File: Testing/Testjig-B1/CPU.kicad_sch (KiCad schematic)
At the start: 7 parts

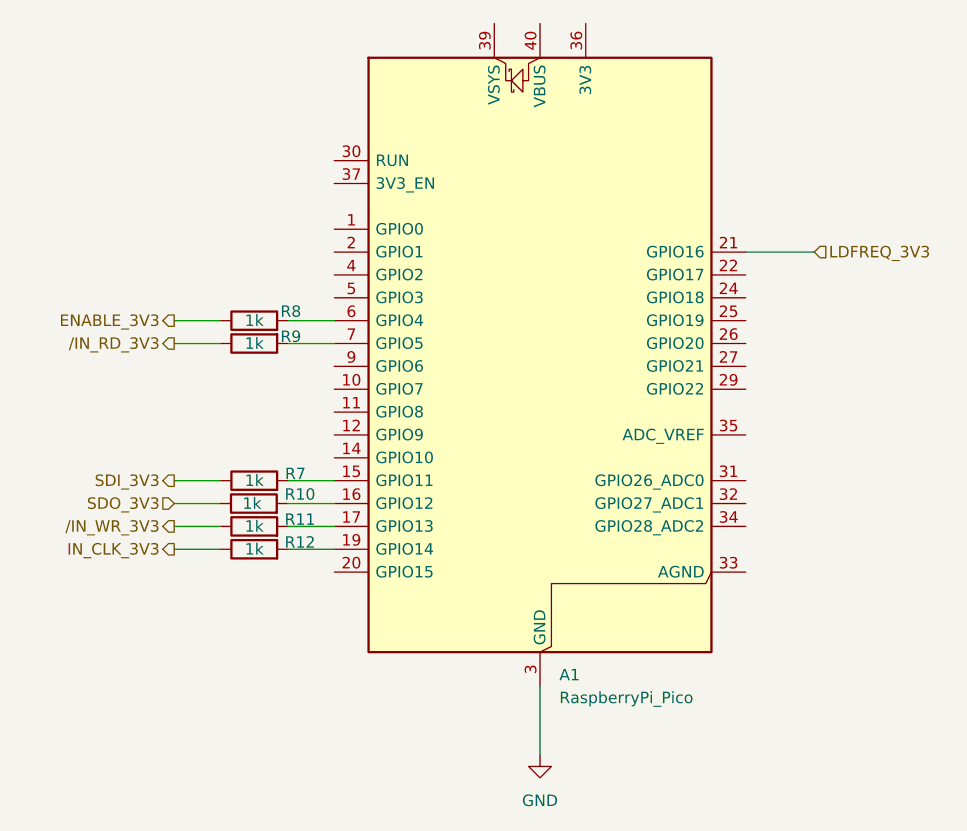
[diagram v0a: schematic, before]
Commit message: First iteration tester design
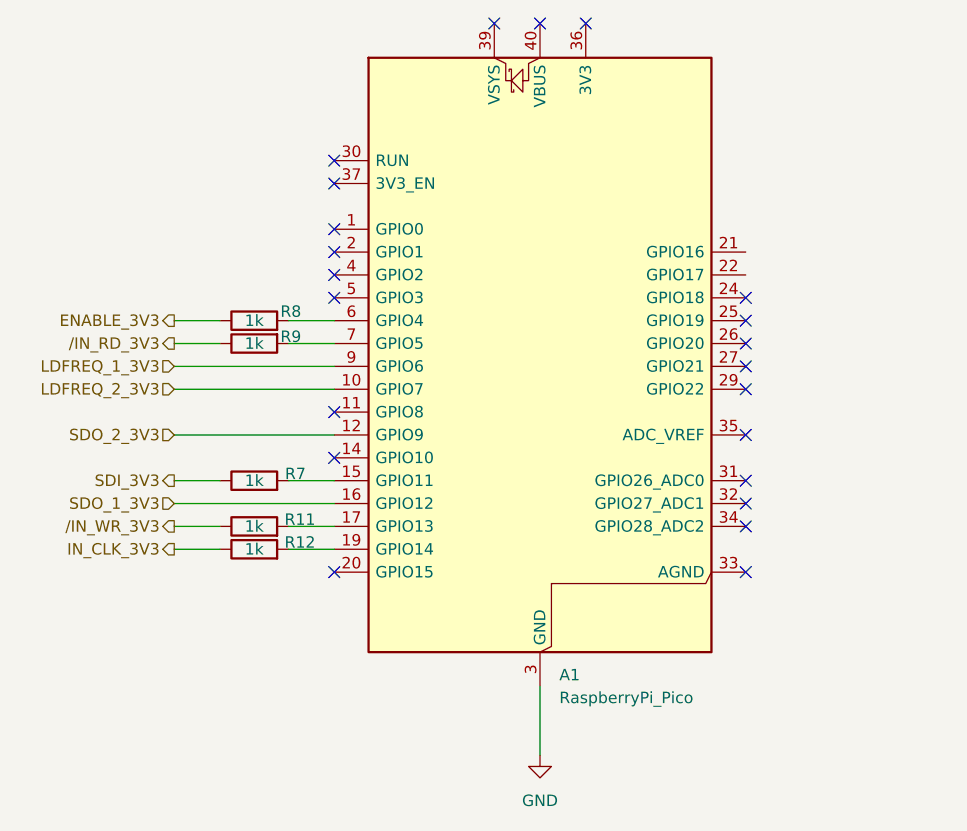
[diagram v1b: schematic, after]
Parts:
- removed R10: 1k, symbol Device:R
- R11, R12, R7, R8, R9: footprint (none) -> Resistor_SMD:R_0805_2012Metric
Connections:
- net LDFREQ_2_3V3: now reaches A1.10 (GPIO7)
- net SDO_2_3V3: now reaches A1.12 (GPIO9)
- net LDFREQ_1_3V3: now reaches A1.9 (GPIO6)
- net LDFREQ_3V3: no longer names the net of A1.21 (GPIO16)
- no-connect marks 0 -> 22
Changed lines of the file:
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@@
 	(generator_version "10.0")
 	(paper "A4")
-	(wire
-		(pts
-			(xy 125.73 69.85) (xy 133.35 69.85)
-		)
-		(stroke
-			(width 0)
-			(type default)
-		)
-	)
-	(wire
-		(pts
-			(xy 74.8862 97.79) (xy 80.01 97.79)
+	(no_connect
+		(at 80.01 69.85)
+	)
+	(no_connect
+		(at 125.73 90.17)
+	)
+	(no_connect
+		(at 125.73 85.09)
+	)
+	(no_connect
+		(at 80.01 87.63)
+	)
+	(no_connect
+		(at 80.01 105.41)
+	)
+	(no_connect
+		(at 107.95 44.45)
+	)
+	(no_connect
+		(at 125.73 77.47)
+	)
+	(no_connect
+		(at 125.73 100.33)
+	)
+	(no_connect
+		(at 125.73 82.55)
+	)
+	(no_connect
+		(at 125.73 80.01)
+	)
+	(no_connect
+		(at 102.87 44.45)
+	)
+	(no_connect
+		(at 125.73 74.93)
+	)
+	(no_connect
+		(at 80.01 59.69)
+	)
+	(no_connect
+		(at 80.01 92.71)
+	)
+	(no_connect
+		(at 80.01 74.93)
+	)
+	(no_connect
+		(at 125.73 97.79)
+	)
+	(no_connect
+		(at 80.01 62.23)
+	)
+	(no_connect
+		(at 80.01 72.39)
+	)
+	(no_connect
+		(at 97.79 44.45)
+	)
+	(no_connect
+		(at 80.01 67.31)
+	)
+	(no_connect
+		(at 125.73 105.41)
+	)
+	(no_connect
+		(at 125.73 95.25)
+	)
+	(wire
+		(pts
+			(xy 80.01 85.09) (xy 62.23 85.09)
 		)
 		(stroke
@@
 	(wire
 		(pts
+			(xy 62.23 90.17) (xy 80.01 90.17)
+		)
+		(stroke
+			(width 0)
+			(type default)
+		)
+	)
+	(wire
+		(pts
+			(xy 80.01 82.55) (xy 62.23 82.55)
+		)
+		(stroke
+			(width 0)
+			(type default)
+		)
+	)
+	(wire
+		(pts
 			(xy 74.93 95.25) (xy 80.01 95.25)
 		)
@@
 		(pts
 			(xy 74.93 80.01) (xy 80.01 80.01)
+		)
+		(stroke
+			(width 0)
+			(type default)
+		)
+	)
+	(wire
+		(pts
+			(xy 67.31 97.79) (xy 80.01 97.79)
 		)
 		(stroke
@@
 		)
 	)
+	(hierarchical_label "LDFREQ_2_3V3"
+		(shape input)
+		(at 62.23 85.09 180)
+		(effects
+			(font
+				(size 1.27 1.27)
+			)
+			(justify right)
+		)
+	)
 	(hierarchical_label "ENABLE_3V3"
 		(shape output)
@@
 		)
 	)
-	(hierarchical_label "LDFREQ_3V3"
+	(hierarchical_label "LDFREQ_1_3V3"
 		(shape input)
-		(at 133.35 69.85 0)
+		(at 62.23 82.55 180)
 		(effects
 			(font
 				(size 1.27 1.27)
 			)
-			(justify left)
+			(justify right)
 		)
 	)
@@
 		)
 	)
-	(hierarchical_label "SDO_3V3"
+	(hierarchical_label "SDO_1_3V3"
 		(shape input)
 		(at 62.23 97.79 180)
@@
 		(shape output)
 		(at 62.23 95.25 180)
+		(effects
+			(font
+				(size 1.27 1.27)
+			)
+			(justify right)
+		)
+	)
+	(hierarchical_label "SDO_2_3V3"
+		(shape input)
+		(at 62.23 90.17 180)
 		(effects
 			(font
@@
 			)
 		)
-		(property "Footprint" ""
+		(property "Footprint" "Resistor_SMD:R_0805_2012Metric"
 			(at 71.12 79.248 90)
 			(hide yes)
@@
 				(path "/ac0bcd9a-6984-47ed-9080-83e8edfb761b/3e980933-0fed-482d-9d01-6233af794343"
 					(reference "R8")
-					(unit 1)
-				)
-			)
-		)
-	)
-	(symbol
-		(lib_id "Device:R")
-		(at 71.0762 97.79 90)
-		(unit 1)
-		(body_style 1)
-		(exclude_from_sim no)
-		(in_bom yes)
-		(on_board yes)
-		(in_pos_files yes)
-		(dnp no)
-		(property "Reference" "R10"
-			(at 76.2 96.774 90)
-			(show_name no)
-			(do_not_autoplace no)
-			(effects
-				(font
-					(size 1.27 1.27)
-				)
-			)
-		)
-		(property "Value" "1k"
-			(at 70.866 97.79 90)
-			(show_name no)
-			(do_not_autoplace no)
-			(effects
-				(font
-					(size 1.27 1.27)
-				)
-			)
-		)
-		(property "Footprint" ""
-			(at 71.0762 99.568 90)
-			(hide yes)
-			(show_name no)
-			(do_not_autoplace no)
-			(effects
-				(font
-					(size 1.27 1.27)
-				)
-			)
-		)
-		(property "Datasheet" ""
-			(at 71.0762 97.79 0)
-			(hide yes)
-			(show_name no)
-			(do_not_autoplace no)
-			(effects
-				(font
-					(size 1.27 1.27)
-				)
-			)
-		)
-		(property "Description" "Resistor"
-			(at 71.0762 97.79 0)
-			(hide yes)
-			(show_name no)
-			(do_not_autoplace no)
-			(effects
-				(font
-					(size 1.27 1.27)
-				)
-			)
-		)
-		(pin "1"
-		)
-		(pin "2"
-		)
-		(instances
-			(project "Testjig-B1"
-				(path "/ac0bcd9a-6984-47ed-9080-83e8edfb761b/3e980933-0fed-482d-9d01-6233af794343"
-					(reference "R10")
 					(unit 1)
 				)
@@
 			)
 		)
-		(property "Footprint" ""
+		(property "Footprint" "Resistor_SMD:R_0805_2012Metric"
 			(at 71.12 102.108 90)
 			(hide yes)
@@
 			)
 		)
-		(property "Footprint" ""
+		(property "Footprint" "Resistor_SMD:R_0805_2012Metric"
 			(at 71.12 78.232 90)
 			(hide yes)
@@
 			)
 		)
-		(property "Footprint" ""
+		(property "Footprint" "Resistor_SMD:R_0805_2012Metric"
 			(at 71.12 104.648 90)
 			(hide yes)
@@
 			)
 		)
-		(property "Footprint" ""
+		(property "Footprint" "Resistor_SMD:R_0805_2012Metric"
 			(at 71.12 97.028 90)
 			(hide yes)

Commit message: Last fixes before production of Rev A.
- Add signal line for SDO1 which had a break in the schematic.
- Route out said signal
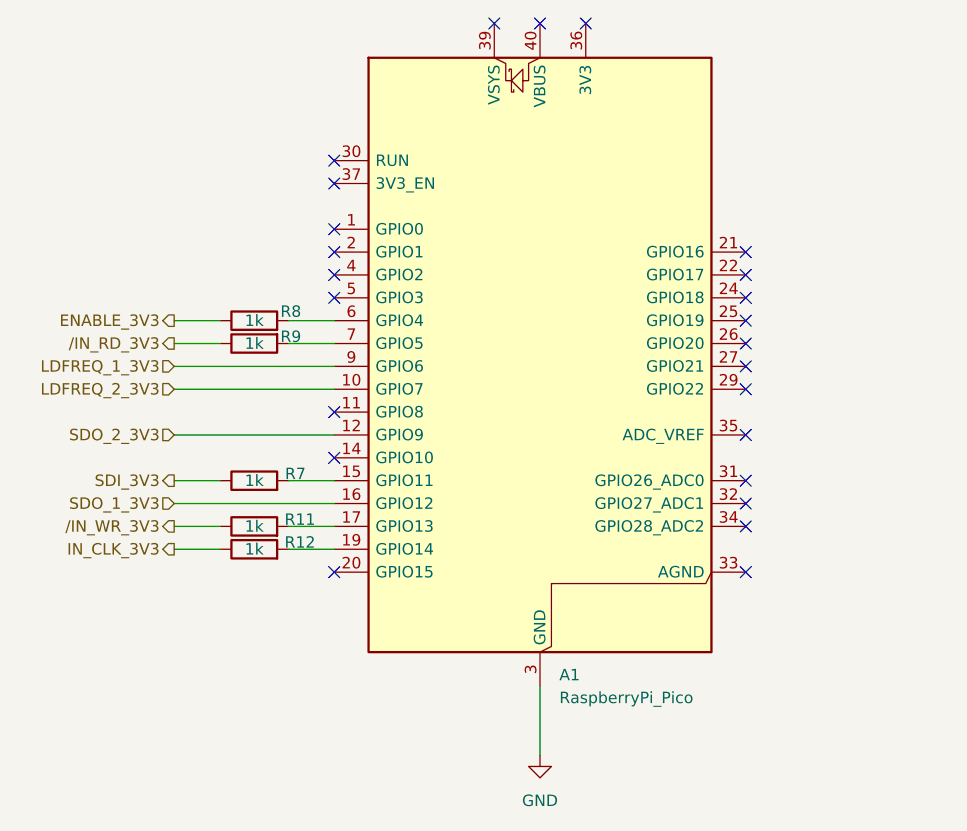
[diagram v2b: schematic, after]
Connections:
- net SDO_1_3V3: now also A1.16 (GPIO12)
- no-connect marks 22 -> 24
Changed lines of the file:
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@@
 	(paper "A4")
+	(no_connect
+		(at 125.73 72.39)
+	)
 	(no_connect
 		(at 80.01 69.85)
@@
 	(no_connect
 		(at 125.73 85.09)
+	)
+	(no_connect
+		(at 125.73 69.85)
 	)
 	(no_connect
@@
 	(wire
 		(pts
-			(xy 67.31 97.79) (xy 80.01 97.79)
-		)
-		(stroke
-			(width 0)
-			(type default)
-		)
-	)
-	(wire
-		(pts
 			(xy 74.93 77.47) (xy 80.01 77.47)
 		)
@@
 	(wire
 		(pts
-			(xy 62.23 97.79) (xy 67.2662 97.79)
+			(xy 62.23 97.79) (xy 80.01 97.79)
 		)
 		(stroke
